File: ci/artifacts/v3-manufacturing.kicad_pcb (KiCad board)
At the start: 2 copper layers, 240 x 47 mm, 164 parts, among them SW1 TS-1187A-B-A-B, U1 INA3221AIRGVR, U10 74HC595, U11 74HC595, U12 HT7533-1, U2 INA3221AIRGVR, U3 TPS54560DDAR, U4 TPS54560DDAR, U5 CH224K, U6 INA3221AIRGVR, U7 CH32V203F6P6, U8 SN74HC4051DR, U9 SN74HC4051DR

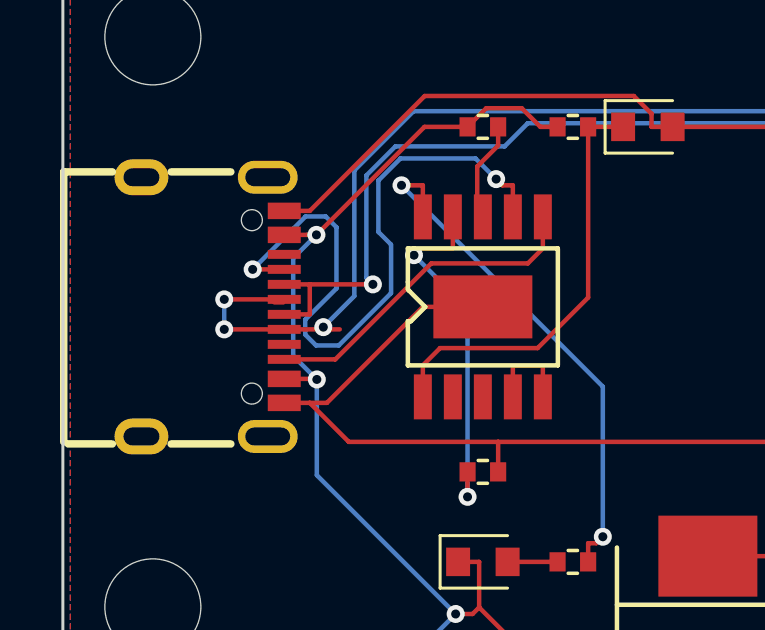
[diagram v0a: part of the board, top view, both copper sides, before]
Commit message: CI: pin the green manufacturing PCB (DRC-clean), not the pre-green route.
v3-routed.kicad_pcb still had USB DP/GND zone overlaps; v3-routed-green is the
artifact that actually passed 0/0 copper DRC.

Co-authored-by: Cursor <cursoragent@cursor.com>
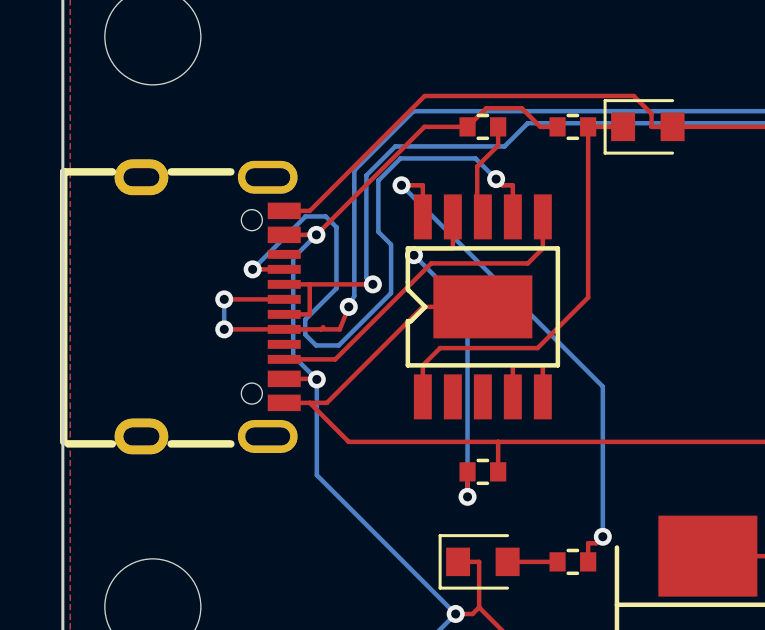
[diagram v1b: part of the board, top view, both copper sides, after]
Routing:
- net usb_dp: track 152.6 -> 151.8 mm

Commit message: Pin manufacturing board from green board:make run
Refresh v3-manufacturing.kicad_pcb from CI run 30182438108
(4a79e92 USB outboard via repair): 0 unconnected, 0 copper errors.

Co-authored-by: Cursor <cursoragent@cursor.com>
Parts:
- R10, R6: value 17.8kΩ -> 17.8kÃÂ©
- R11, R7: value 3.4kΩ -> 3.4kÃÂ©
- R12, R8: value 162kΩ -> 162kÃÂ©
- R13, R14, R17: value 24kΩ -> 24kÃÂ©
- R15, R16, R77: value 100kΩ -> 100kÃÂ©
- R18, R69, R70: value 4.7kΩ -> 4.7kÃÂ©
- R19, R53, R54, R55, R56, R57, R58, R59, R60, R61, R62, R63, R64, R65, R66, R67, R68, R72: value 1kΩ -> 1kÃÂ©
- R20, R21, R24, R25, R28, R29, R32, R33, R36, R37, R40, R41, R44, R45, R48, R49: value 22kΩ -> 22kÃÂ©
- R23, R27, R31, R35, R39, R43, R47, R51: value 100mΩ -> 100mÃÂ©
- R5, R9: value 23.7kΩ -> 23.7kÃÂ©
- R52, R71, R73, R74, R75, R76: value 10kΩ -> 10kÃÂ©
